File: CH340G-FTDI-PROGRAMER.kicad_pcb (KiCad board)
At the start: 2 copper layers, 89.6 x 96.9 mm, 64 parts

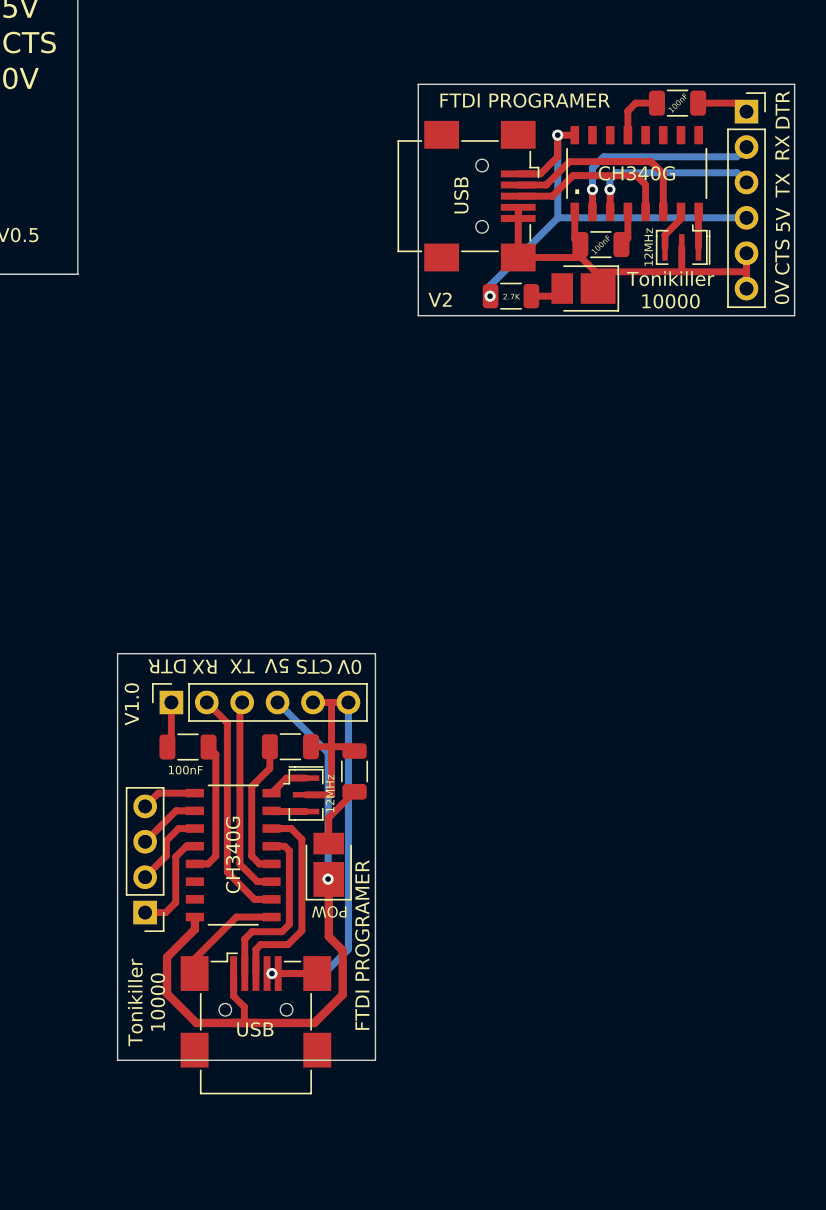
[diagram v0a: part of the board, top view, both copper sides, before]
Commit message: CH340G FTDI Programmer V2.0
The board is ready to order, but I can`t order it rigth now, so I will have to wait about 2 months to finish this project permanently.

So the last version had the D+ and D- reversed, IDK how I did that, and more than that, I inversed the TX and RX pins and not realy. Iconnected the atmega tx to an conexion named rx, expecting ro connect RX to that pin, and same with rx. The same I done with the FTDI, and by doing that, I double reversed the tx and rx wires, so it`s like I didn`t reversed them at all.
In all that tests I saw that the 100nF capacitor at the DTR is not necesarry, and it could be just a wire in it`s place, and more than that, could be added some design changes... round corners, holes for a case, tx and rx yellow led`s, and stuff like this.
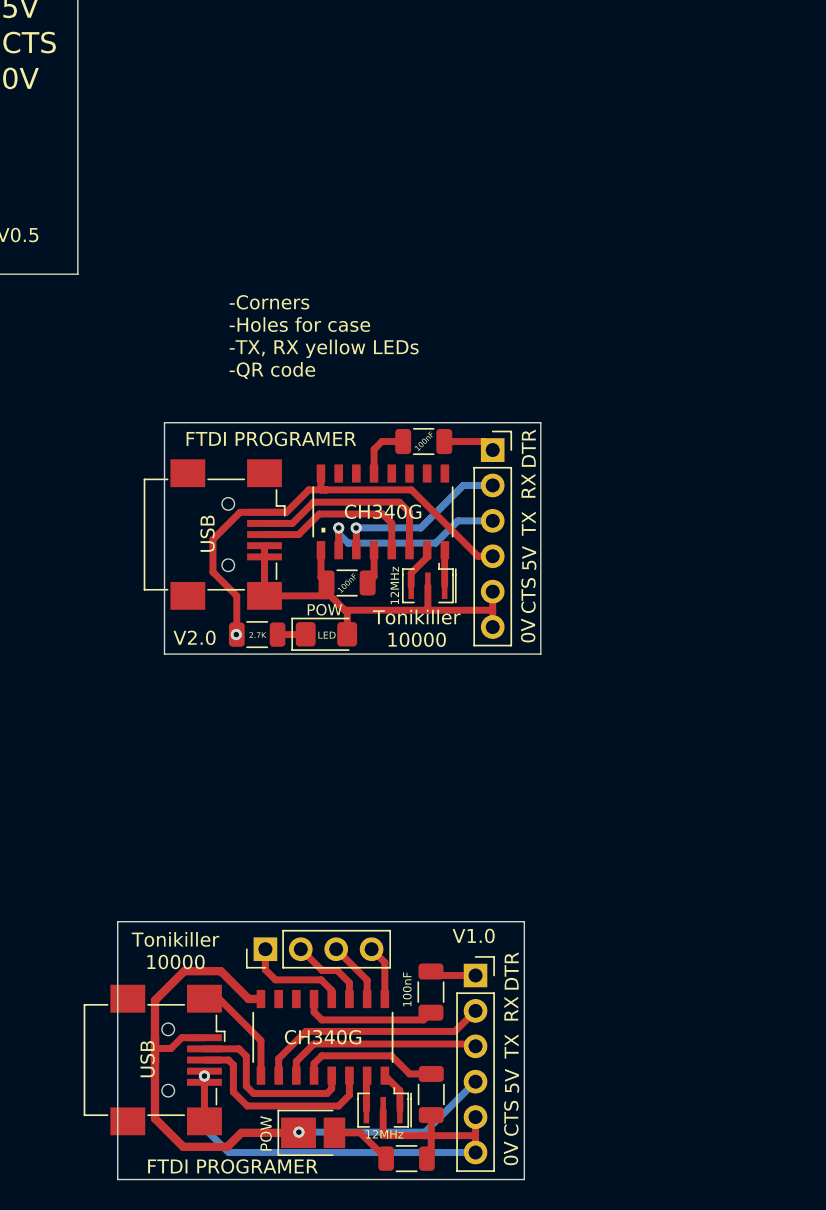
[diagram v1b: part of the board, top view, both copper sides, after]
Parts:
- removed the REF** at (198.3, 93.0)
- added LED: LED_1206_3216Metric_Pad1.42x1.75mm_HandSolder, LED_SMD:LED_1206_3216Metric_Pad1.42x1.75mm_HandSolder, F.Cu at (179.9, 117.9)
- moved 100nF 30.4 mm to (186.9, 104.0)
- moved 100nF 30.4 mm to (181.4, 114.2)
- moved 12MHz 30.4 mm to (187.2, 114.4)
- moved 2.7K 30.4 mm to (174.9, 117.9)
- moved CH340G 30.4 mm to (184.0, 109.1)
- moved REF** 30.4 mm to (191.8, 104.6)
- moved USB 30.3 mm to (172.9, 110.7)
- moved G*** 29.8 mm to (203.6, 135.0)
- moved REF** 29.3 mm to (190.6, 142.3), turned to 0 degrees
- moved 1K 28.0 mm to (185.7, 155.5), turned to 180 degrees
- moved 100nF 26.9 mm to (187.4, 150.9), turned to 90 degrees
- moved 100nF 24.8 mm to (187.4, 143.5), turned to -90 degrees
- moved 12MHz 23.3 mm to (184.0, 152.0), turned to 180 degrees
- moved REF** 19.3 mm to (179.0, 153.6), turned to 0 degrees
- moved CH340G 14.6 mm to (179.7, 146.8), turned to 90 degrees
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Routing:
- net (no net): track 1169.9 -> 1168.5 mm, vias 18 -> 17
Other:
- board size 89.6 x 96.9 mm -> 71.4 x 96.9 mm
- board text added: "-Corners -Holes for case -TX, RX yellow LEDs -QR code"
- board text added: "V2.0"
- board text removed: "V2"

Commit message: V2
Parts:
- added 100nF: 100nF, Capacitor_SMD:C_1206_3216Metric, F.Cu at (172.5, 150.9)
- added 100nF: C_1206_3216Metric, Capacitor_SMD:C_1206_3216Metric, F.Cu at (178.0, 140.8)
- added 12MHz: Resonator_SMD_Murata_CSTxExxV-3Pin_3.0x1.1mm, Crystal:Resonator_SMD_Murata_CSTxExxV-3Pin_3.0x1.1mm, F.Cu at (178.3, 151.1)
- added 2.7K: 2.7K, Resistor_SMD:R_1206_3216Metric, F.Cu at (166.1, 154.6)
- added CH340G: SOIC127P600X180-16N, SOIC127P600X180-16N, F.Cu at (175.1, 145.8)
- added G***: LOGO, LOGO, B.Cu at (228.1, 131.1)
- added LED: LED_1206_3216Metric_Pad1.42x1.75mm_HandSolder, LED_SMD:LED_1206_3216Metric_Pad1.42x1.75mm_HandSolder, F.Cu at (171.1, 154.6)
- added REF**: PinSocket_1x06_P2.54mm_Vertical, Connector_PinSocket_2.54mm:PinSocket_1x06_P2.54mm_Vertical, F.Cu at (185.9, 141.4)
- added USB: USB_Mini-B_Wuerth_65100516121_Horizontal, Connector_USB:USB_Mini-B_Wuerth_65100516121_Horizontal, F.Cu at (164.0, 147.4)
- moved REF** 41.9 mm to (170.4, 98.9)
- moved 100nF 41.9 mm to (182.3, 102.0)
- moved 12MHz 41.9 mm to (178.9, 110.4)
- moved CH340G 41.9 mm to (174.6, 105.2)
- moved REF** 41.9 mm to (185.5, 100.8)
- moved USB 41.9 mm to (163.5, 106.8)
- moved 100nF 41.9 mm to (182.3, 109.3)
- moved 1K 41.9 mm to (180.6, 113.9)
- moved REF** 41.9 mm to (173.9, 112.1)
- moved 12MHz 17.5 mm to (179.6, 130.1)
- moved 2.7K 17.5 mm to (167.3, 133.6)
- moved CH340G 17.5 mm to (176.3, 124.8)
- moved REF** 17.5 mm to (184.2, 120.4)
- moved USB 17.5 mm to (165.2, 126.4)
- moved 100nF 17.5 mm to (179.3, 119.7)
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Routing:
- net (no net): track 1168.5 -> 1316.4 mm, vias 17 -> 20
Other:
- board size 71.4 x 96.9 mm -> 65.6 x 96.9 mm
- board text added: "V1.6"
- board text removed: "-Corners -Holes for case -TX, RX yellow LEDs -QR code"

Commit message: qq
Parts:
- removed the G*** at (204.1, 84.7)
- removed the G*** at (203.6, 135.0)
- added C3: 100uF, Capacitor_SMD:C_1210_3225Metric_Pad1.33x2.70mm_HandSolder, B.Cu at (206.9, 152.3)
- added C4: 100nF, Capacitor_SMD:C_1206_3216Metric, F.Cu at (210.5, 150.8)
- added C5: 100uF, Capacitor_SMD:C_1210_3225Metric_Pad1.33x2.70mm_HandSolder, B.Cu at (206.9, 143.8)
- added C6: 100nF, Capacitor_SMD:C_1206_3216Metric, F.Cu at (222.6, 140.8)
- added D1: RED, LED_SMD:LED_1206_3216Metric_Pad1.42x1.75mm_HandSolder, F.Cu at (223.1, 151.6)
- added G***: LOGO, LOGO, B.Cu at (218.1, 147.4)
- added J1: USB, Connector_USB:USB_Mini-B_Wuerth_65100516121_Horizontal, F.Cu at (202.8, 148.5)
- added J2: PINS, Connector_PinHeader_2.54mm:PinHeader_1x04_P2.54mm_Vertical, F.Cu at (211.9, 140.3)
- added J3: Conn_01x03_Pin, Connector_PinHeader_2.54mm:PinHeader_1x03_P2.54mm_Vertical, F.Cu at (200.3, 140.6)
- added J4: Conn_01x06_Pin, Connector_PinSocket_2.54mm:PinSocket_1x06_P2.54mm_Vertical, F.Cu at (227.1, 140.3)
- added R1: 1K, Resistor_SMD:R_1206_3216Metric, F.Cu at (220.7, 151.5)
- added R2: 1K, Resistor_SMD:R_1206_3216Metric, F.Cu at (221.9, 147.4)
- added R3: 1K, Resistor_SMD:R_1206_3216Metric, F.Cu at (221.8, 145.1)
- added U1: AMS1117-3.3, 78L05:PK(R-PSSO-F3), B.Cu at (204.8, 148.0)
- added U2: CH340G, SOIC127P600X180-16N, F.Cu at (213.1, 145.9)
- added Y1: 12MHz, Crystal:Resonator_SMD_Murata_CSTxExxV-3Pin_3.0x1.1mm, F.Cu at (216.3, 151.2)
- moved G*** 51.5 mm to (178.1, 143.5)
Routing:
- net (no net): track 1316.4 -> 1589.8 mm, vias 20 -> 21
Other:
- board size 65.6 x 96.9 mm -> 105.3 x 96.9 mm
- board text added: "3.3V"
- board text added: "GND"
- board text added: "V2.1"
- board text added: "VCC"
- board text removed: "MK1 V1.0"

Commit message: u
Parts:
- added C1: 10uF, Capacitor_SMD:C_0603_1608Metric, F.Cu at (265.1, 118.9)
- added C3: 100uF, Capacitor_SMD:C_1210_3225Metric_Pad1.33x2.70mm_HandSolder, B.Cu at (272.7, 121.0)
- added C4: 100nF, Capacitor_SMD:C_1206_3216Metric, F.Cu at (220.6, 112.9)
- added C5: 100uF, Capacitor_SMD:C_1210_3225Metric_Pad1.33x2.70mm_HandSolder, B.Cu at (272.7, 112.5)
- added C6: 100nF, Capacitor_SMD:C_0603_1608Metric_Pad1.08x0.95mm_HandSolder, F.Cu at (265.1, 131.4)
- added C6: 100nF, Capacitor_SMD:C_0603_1608Metric_Pad1.08x0.95mm_HandSolder, F.Cu at (255.8, 122.5)
- added C6: 100nF, Capacitor_SMD:C_0603_1608Metric_Pad1.08x0.95mm_HandSolder, F.Cu at (232.6, 102.8)
- added D1: POW, LED_SMD:LED_0603_1608Metric_Pad1.05x0.95mm_HandSolder, F.Cu at (253.6, 131.4)
- added D1: RED, LED_SMD:LED_1206_3216Metric_Pad1.42x1.75mm_HandSolder, F.Cu at (233.2, 113.7)
- added J1: USB, Connector_USB:USB_Mini-B_Wuerth_65100516121_Horizontal, F.Cu at (212.8, 110.6)
- added J2: USB_C_USB2.0, Connector_USB:USB_C_Receptacle_HRO_TYPE-C-31-M-12, F.Cu at (260.5, 110.7)
- added J3: Conn_01x03_Pin, Connector_PinHeader_2.54mm:PinHeader_1x03_P2.54mm_Vertical, F.Cu at (210.3, 102.7)
- added J4: Conn_01x06_Pin, Connector_PinSocket_2.54mm:PinSocket_1x06_P2.54mm_Vertical, F.Cu at (265.1, 135.2)
- added J4: Conn_01x06_Pin, Connector_PinSocket_2.54mm:PinSocket_1x06_P2.54mm_Vertical, F.Cu at (237.2, 102.4)
- added R1: 1K, Resistor_SMD:R_1206_3216Metric, F.Cu at (230.8, 113.7)
- added R2: 1K, Resistor_SMD:R_1206_3216Metric, F.Cu at (231.9, 109.6)
- added R3: 1K, Resistor_SMD:R_0603_1608Metric_Pad0.98x0.95mm_HandSolder, F.Cu at (257.4, 130.5)
- added R3: 1K, Resistor_SMD:R_0603_1608Metric_Pad0.98x0.95mm_HandSolder, F.Cu at (260.0, 130.5)
- added R3: 1K, Resistor_SMD:R_0603_1608Metric_Pad0.98x0.95mm_HandSolder, F.Cu at (262.6, 130.5)
- added R3: 5K1, Resistor_SMD:R_0603_1608Metric, F.Cu at (262.7, 116.9)
- added R3: 1K, Resistor_SMD:R_1206_3216Metric, F.Cu at (231.9, 107.2)
- added R4: 5K1, Resistor_SMD:R_0603_1608Metric, F.Cu at (258.0, 116.8)
- added REF**: TestPoint_Pad_1.0x1.0mm, TestPoint:TestPoint_Pad_1.0x1.0mm, F.Cu at (265.2, 123.0)
- added REF**: TestPoint_Pad_1.0x1.0mm, TestPoint:TestPoint_Pad_1.0x1.0mm, F.Cu at (265.2, 124.8)
- added REF**: TestPoint_Pad_1.0x1.0mm, TestPoint:TestPoint_Pad_1.0x1.0mm, F.Cu at (265.2, 126.5)
- added REF**: TestPoint_Pad_1.0x1.0mm, TestPoint:TestPoint_Pad_1.0x1.0mm, F.Cu at (265.2, 128.3)
- added SW1: MSK12C02, MSK12C02:MSK12C02, F.Cu at (252.2, 118.0)
- added U1: AMS1117-3.3, 78L05:PK(R-PSSO-F3), B.Cu at (270.6, 116.7)
- added U2: CH340G, SOIC127P600X180-16N, F.Cu at (260.4, 123.1)
- added U2: CH340G, SOIC127P600X180-16N, F.Cu at (223.1, 108.0)
- added Y1: 12MHz, Crystal:Resonator_SMD_Murata_CSTxExxV-3Pin_3.0x1.1mm, F.Cu at (226.3, 113.3)
- added Y1: 12MHz, Crystal:Resonator_SMD_Murata_CSTxExxV-3Pin_3.0x1.1mm, F.Cu at (255.3, 127.6)
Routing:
- net (no net): track 1589.8 -> 1977.6 mm, vias 21 -> 23
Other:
- board size 105.3 x 96.9 mm -> 143.1 x 96.9 mm
- board text added: "JLCJLCJLCJLC"
- board text added: "V3.0"
